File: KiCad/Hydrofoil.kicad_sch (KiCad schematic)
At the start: 19 parts, among them J1 Conn_01x05_Pin, U1 LM334M, U2 LM334M, U3 ADS1115IDGS

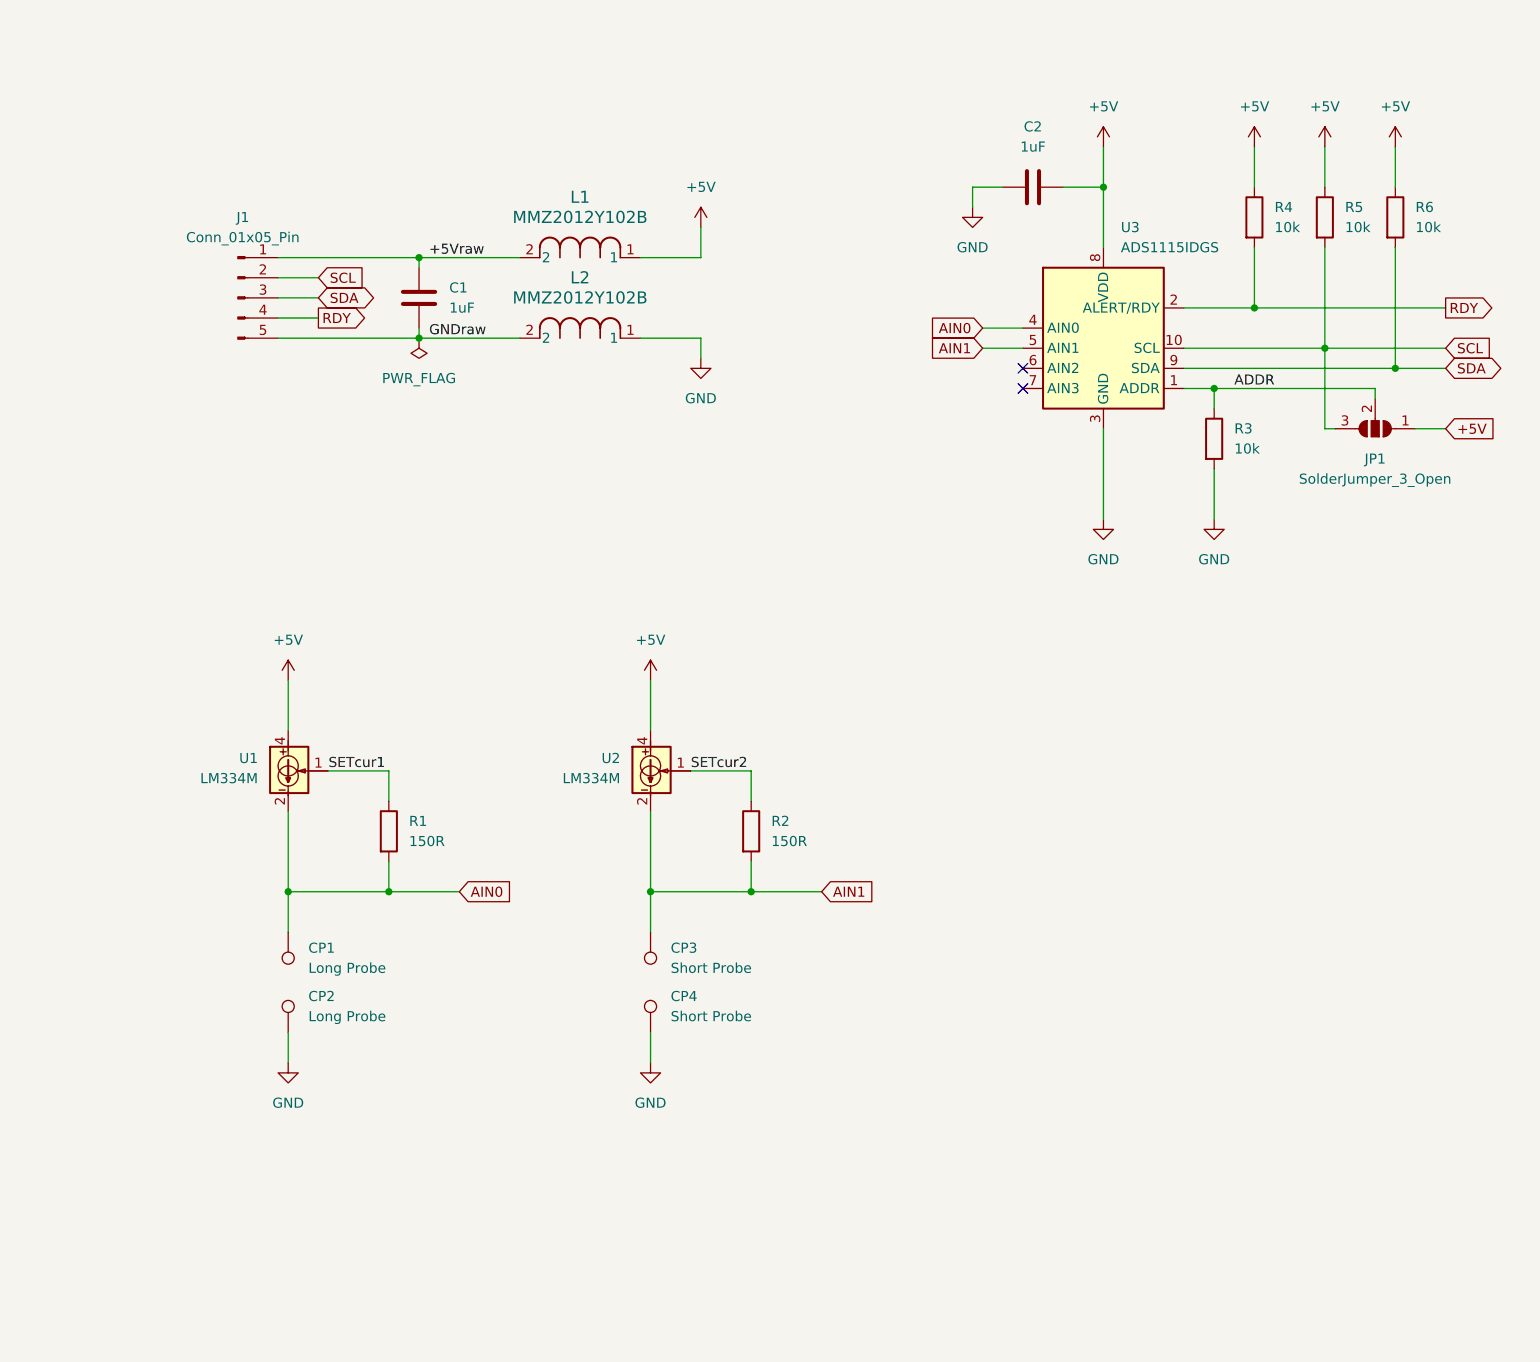
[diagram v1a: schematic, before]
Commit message: Add PS to the curcuit, change PCB outline
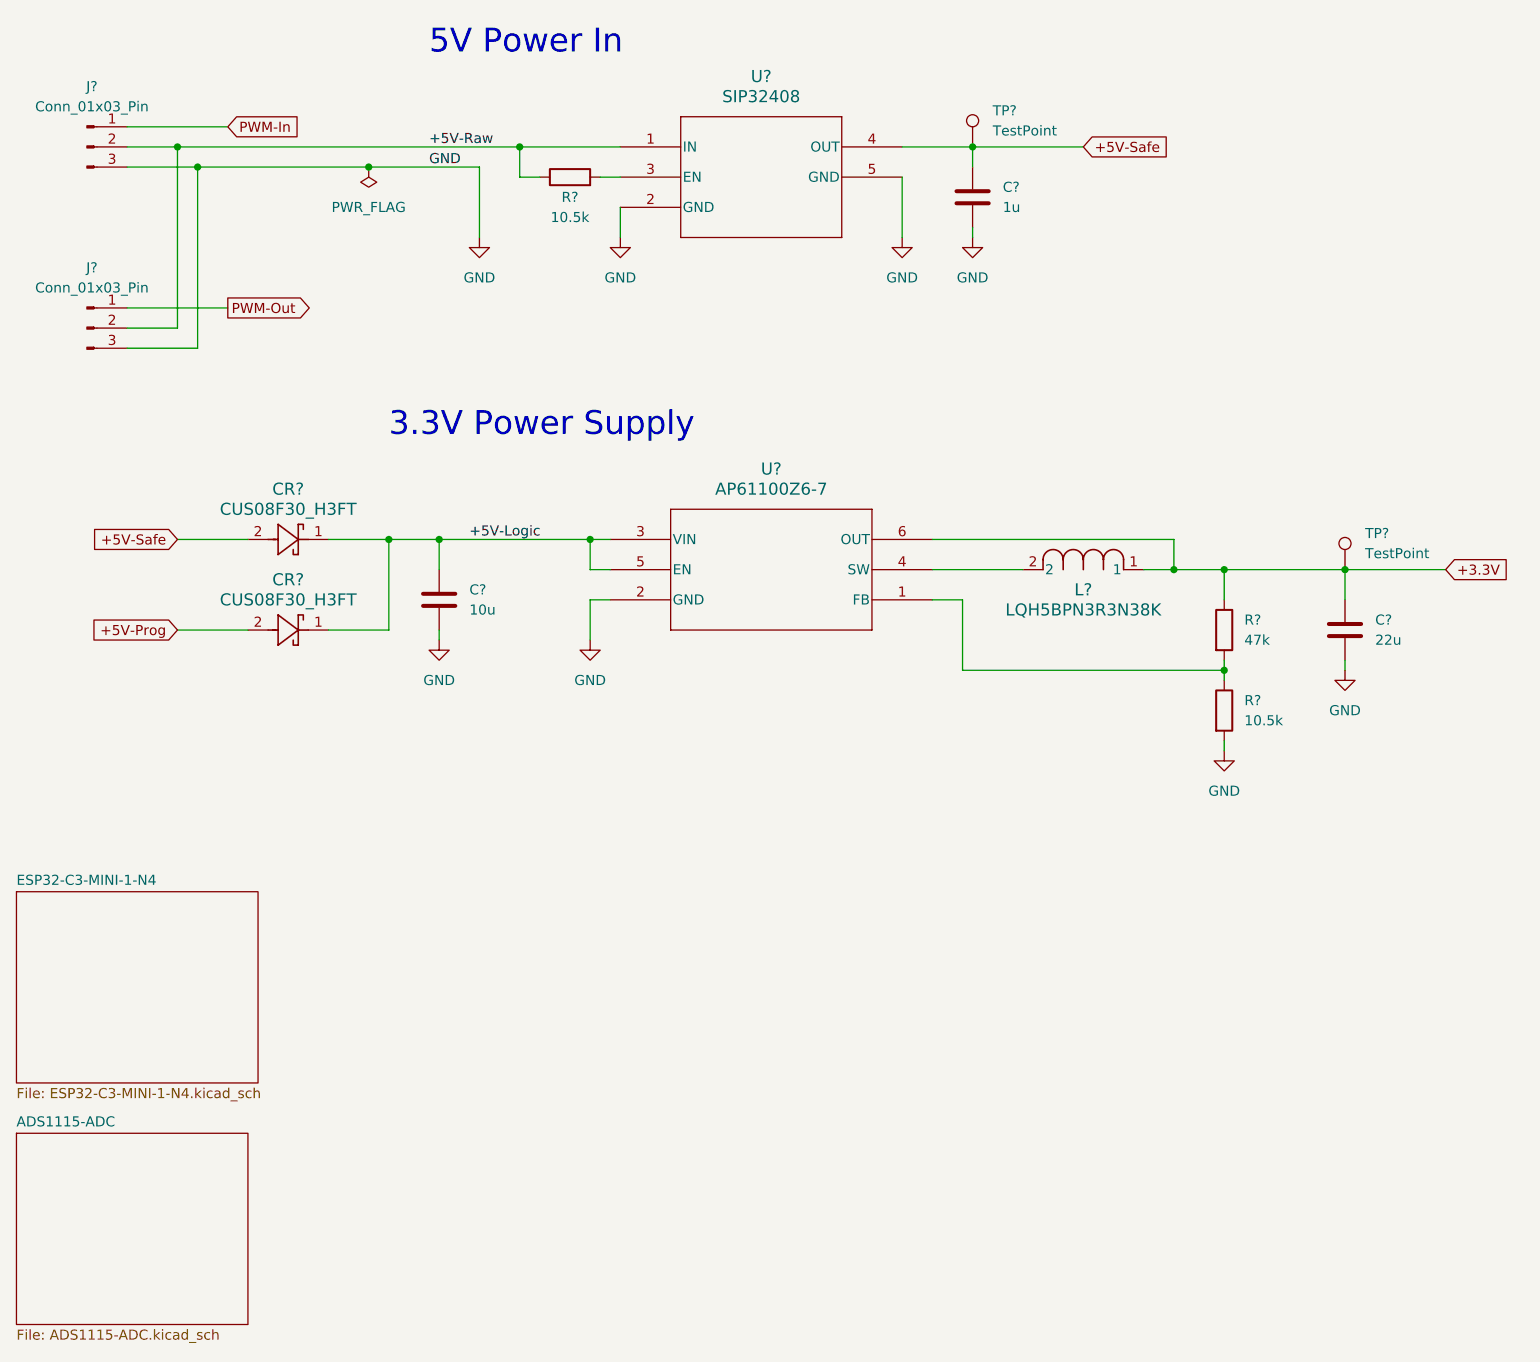
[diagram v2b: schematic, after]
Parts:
- removed C1, C2: 1uF, Capacitor_SMD:C_1206_3216Metric_Pad1.33x1.80mm_HandSolder, symbol Device:C
- removed CP1, CP2: Long Probe, TestPoint:TestPoint_Pad_D2.0mm, symbol Connector:TestPoint
- removed CP3, CP4: Short Probe, TestPoint:TestPoint_Pad_D2.0mm, symbol Connector:TestPoint
- removed J1: Conn_01x05_Pin, Connector_PinHeader_2.54mm:PinHeader_1x05_P2.54mm_Horizontal, symbol Connector:Conn_01x05_Pin
- removed JP1: SolderJumper_3_Open, Jumper:SolderJumper-3_P1.3mm_Open_RoundedPad1.0x1.5mm, symbol Jumper:SolderJumper_3_Open
- removed L1, L2: MMZ2012Y102B, Inductor_SMD:L_0805_2012Metric_Pad1.05x1.20mm_HandSolder, symbol 2023-09-04_18-15-31:MMZ2012Y102B
- removed R1, R2: 150R, Resistor_SMD:R_1206_3216Metric_Pad1.30x1.75mm_HandSolder, symbol Device:R
- removed R3, R4, R5, R6: 10k, Resistor_SMD:R_1206_3216Metric_Pad1.30x1.75mm_HandSolder, symbol Device:R
- removed U1, U2: LM334M, Package_SO:SOIC-8_3.9x4.9mm_P1.27mm, symbol Reference_Current:LM334M
- removed U3: ADS1115IDGS, Package_SO:TSSOP-10_3x3mm_P0.5mm, symbol Analog_ADC:ADS1115IDGS
- added C?: 1u, Capacitor_SMD:C_0402_1005Metric_Pad0.74x0.62mm_HandSolder, symbol Device:C
- added C?: 10u, Capacitor_SMD:C_0805_2012Metric_Pad1.18x1.45mm_HandSolder, symbol Device:C
- added C?: 22u, Capacitor_SMD:C_0805_2012Metric_Pad1.18x1.45mm_HandSolder, symbol Device:C
- added CR? (x2): CUS08F30_H3FT, USC_TOS, symbol 2023-10-06_10-19-56:CUS08F30_H3FT
- added J? (x2): Conn_01x03_Pin, symbol Connector:Conn_01x03_Pin
- added L?: LQH5BPN3R3N38K, LQH5BPN3R3N38K:IND_LQH5BPN_MUR, symbol 2023-10-06_11-24-05:LQH5BPN3R3N38K
- added R?: 47k, Resistor_SMD:R_0402_1005Metric_Pad0.72x0.64mm_HandSolder, symbol Device:R
- added R? (x2): 10.5k, Resistor_SMD:R_0402_1005Metric_Pad0.72x0.64mm_HandSolder, symbol Device:R
- added TP? (x2): TestPoint, symbol Connector:TestPoint
- added U?: SIP32408, footprints:TDFN_8DNP-T1-GE4_VIS, symbol 2023-10-06_09-07-39:SIP32408DNP-T1-GE4
- added U?: AP61100Z6-7, SOT563-Z6_DIO, symbol 2023-10-06_10-32-16:AP61100Z6-7
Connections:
- net GND: now also C?.2, C?.2, C?.2, J?.3 (Pin_3), J?.3 (Pin_3), R?.2, U?.2 (GND), U?.2 (GND), U?.5 (GND)
- new net: R?.2, U?.3 (EN)
- new net: R?.1, R?.2, U?.1 (FB)
- new net: L?.2, U?.4 (SW)
- new net +3.3V: C?.1, L?.1, R?.1, TP?.1, U?.6 (OUT)
- new net +5V-Logic: C?.1, CR?.1, CR?.1, U?.3 (VIN), U?.5 (EN)
- new net +5V-Prog: CR?.2
- new net +5V-Raw: J?.2 (Pin_2), J?.2 (Pin_2), R?.1, U?.1 (IN)
- new net +5V-Safe: C?.1, CR?.2, TP?.1, U?.4 (OUT)
- new net PWM-In: J?.1 (Pin_1)
- new net PWM-Out: J?.1 (Pin_1)
- no-connect marks 2 -> 0
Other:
- added sheet ADS1115-ADC (ADS1115-ADC.kicad_sch)
- added sheet ESP32-C3-MINI-1-N4 (ESP32-C3-MINI-1-N4.kicad_sch)
- note added: "3.3V Power Supply"
- note added: "5V Power In"

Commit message: Add ESP32-C3-Mini
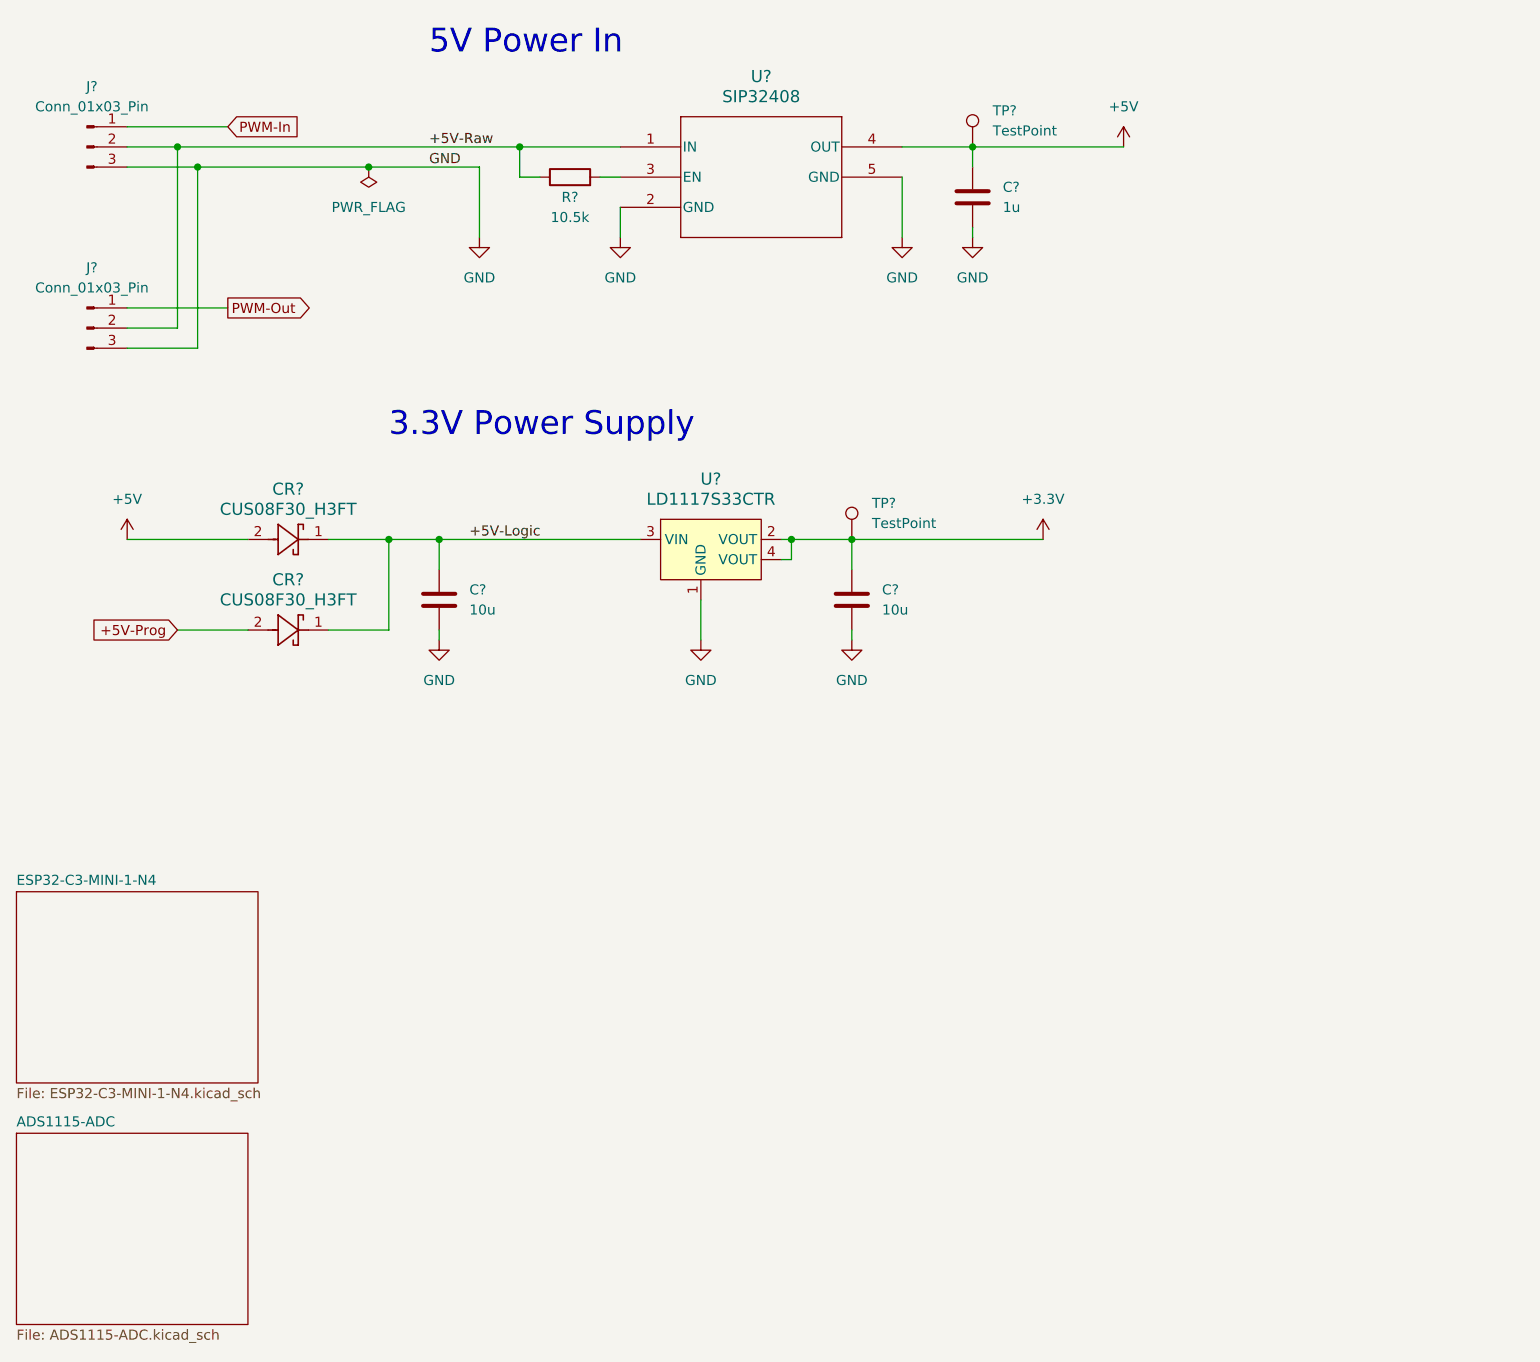
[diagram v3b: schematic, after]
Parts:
- removed C?: 22u, Capacitor_SMD:C_0805_2012Metric_Pad1.18x1.45mm_HandSolder, symbol Device:C
- removed L?: LQH5BPN3R3N38K, LQH5BPN3R3N38K:IND_LQH5BPN_MUR, symbol 2023-10-06_11-24-05:LQH5BPN3R3N38K
- removed R?: 47k, Resistor_SMD:R_0402_1005Metric_Pad0.72x0.64mm_HandSolder, symbol Device:R
- removed R?: 10.5k, Resistor_SMD:R_0402_1005Metric_Pad0.72x0.64mm_HandSolder, symbol Device:R
- removed TP?: TestPoint, symbol Connector:TestPoint
- removed U?: AP61100Z6-7, SOT563-Z6_DIO, symbol 2023-10-06_10-32-16:AP61100Z6-7
- added C?: 10u, Capacitor_SMD:C_0805_2012Metric_Pad1.18x1.45mm_HandSolder, symbol Device:C
- added TP?: TestPoint, symbol Connector:TestPoint
- added U?: LD1117S33CTR, digikey-footprints:SOT-223, symbol dk_PMIC-Voltage-Regulators-Linear:LD1117S33CTR
- CR? (x2): footprint USC_TOS -> CUS08F30:USC_TOS
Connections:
- net +3.3V: now also C?.1, TP?.1, U?.2 (VOUT), U?.4 (VOUT)
- net +5V-Logic: now also U?.3 (VIN)
- net GND: now also C?.2, U?.1 (GND)
- net +5V-Safe renamed +5V

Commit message: Add level shifters
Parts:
- gave numbers to parts that had none: 12
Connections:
- net PWM-In renamed PWM-In-HV
- net PWM-Out renamed PWM-Out-HV

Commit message: Change resistor values
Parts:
- R1: value 10.5k -> 10k

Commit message: Change reverse polarity protection, start the PCB design
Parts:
- removed R1: 10k, Resistor_SMD:R_0402_1005Metric_Pad0.72x0.64mm_HandSolder, symbol Device:R
- removed U2: SIP32408, footprints:TDFN_8DNP-T1-GE4_VIS, symbol 2023-10-06_09-07-39:SIP32408DNP-T1-GE4
- added D1: BZV55B7V5, Diode_SMD:D_MiniMELF, symbol Diode:BZV55B7V5
- added Q1: AO3413, Package_TO_SOT_SMD:SOT-23, symbol Custom-Library:AO3413
- added R6: 100k, Resistor_SMD:R_0402_1005Metric_Pad0.72x0.64mm_HandSolder, symbol Device:R
- C1: footprint Capacitor_SMD:C_0805_2012Metric_Pad1.18x1.45mm_HandSolder -> Capacitor_SMD:C_0402_1005Metric_Pad0.74x0.62mm_HandSolder
- C2: renamed from C3; value 1u -> 10u
- C3: renamed from C2; footprint Capacitor_SMD:C_0805_2012Metric_Pad1.18x1.45mm_HandSolder -> Capacitor_SMD:C_0402_1005Metric_Pad0.74x0.62mm_HandSolder
- J1, J2: footprint (none) -> Custom_Footprints:Solder_Connector
- TP1: renamed from TP2; footprint (none) -> TestPoint:TestPoint_Pad_D1.5mm
- TP2: renamed from TP1; footprint (none) -> TestPoint:TestPoint_Pad_D1.5mm
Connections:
- net +5V: now also D1.1 (K), Q1.2
- net +5V-Raw: now also Q1.3
- net GND: now also R6.2
- new net: D1.2 (A), Q1.1, R6.1
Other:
- moved on the sheet: C2, C3, TP1, TP2

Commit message: Use load switch, fix TC2030 pins, fix strapping pins
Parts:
- removed D1: BZV55B7V5, Diode_SMD:D_MiniMELF, symbol Diode:BZV55B7V5
- removed Q1: AO3413, Package_TO_SOT_SMD:SOT-23, symbol Custom-Library:AO3413
- removed R6: 100k, Resistor_SMD:R_0402_1005Metric_Pad0.72x0.64mm_HandSolder, symbol Device:R
- added R2: 10k, Resistor_SMD:R_0402_1005Metric_Pad0.72x0.64mm_HandSolder, symbol Device:R
- added U2: TPS22917DBV, Package_TO_SOT_SMD:SOT-23-6, symbol Power_Management:TPS22917DBV
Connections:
- net +5V: now also U2.6 (VOUT)
- net +5V-Raw: now also R2.2, U2.1 (VIN)
- net GND: now also U2.2 (GND)
- new net: R2.1, U2.3 (ON)
- no-connect marks 0 -> 2
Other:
- moved on the sheet: C2, TP1

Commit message: Organize parts on the PCB
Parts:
- removed TP1, TP2: TestPoint, TestPoint:TestPoint_Pad_D1.5mm, symbol Connector:TestPoint
- renumbered C1 to C4, C2 to C5, C3 to C6, CR1 to CR3, CR2 to CR4, U1 to U2, U2 to U3
